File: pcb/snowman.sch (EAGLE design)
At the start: 15 parts, among them U1 ATTINY85-20PU

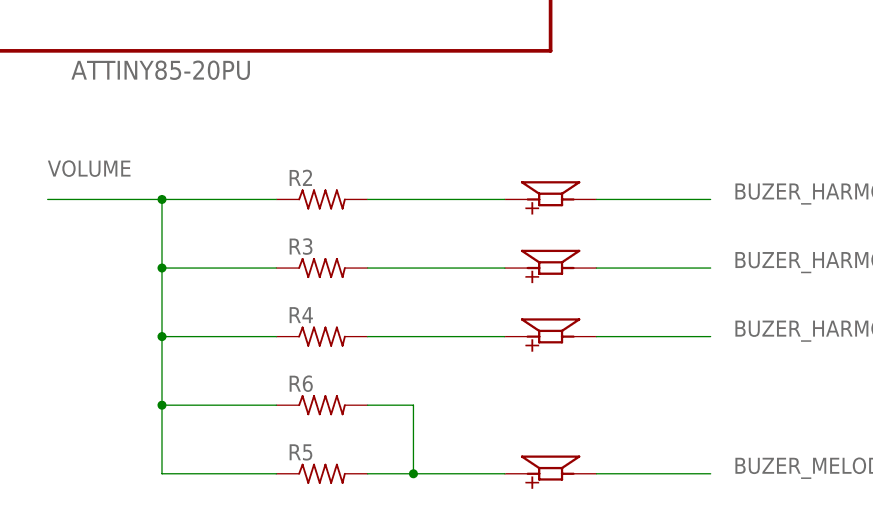
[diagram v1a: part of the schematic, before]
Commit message: add diode current filter to buzzers
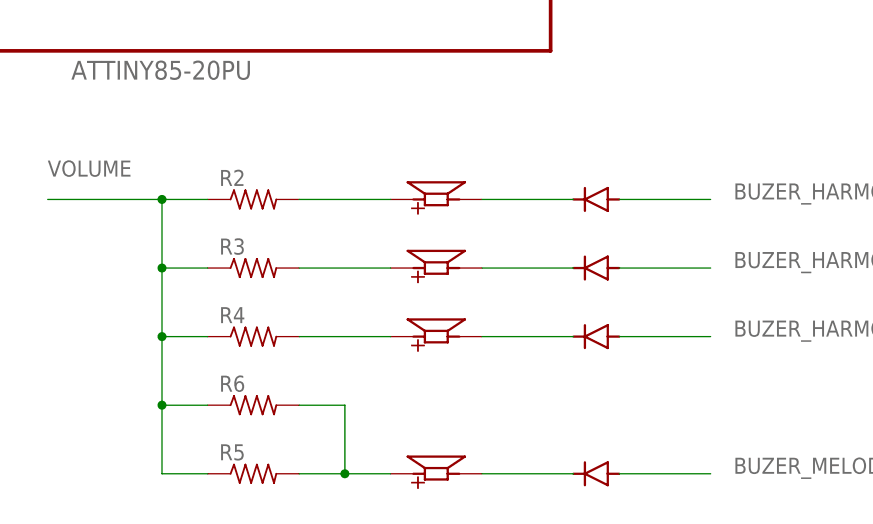
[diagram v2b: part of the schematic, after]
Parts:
- added D1, D2, D3, D4: GF1, diode:GF1
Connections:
- new net N$10: D1.C, LS1.N
- new net N$7: D4.C, LS2.N
- new net N$8: D3.C, LS4.N
- new net N$9: D2.C, LS3.N
- net BUZER_HARMONY_1: now also D4.A; no longer LS2.N
- net BUZER_HARMONY_2: now also D3.A; no longer LS4.N
- net BUZER_HARMONY_3: now also D2.A; no longer LS3.N
- net BUZER_MELODY: now also D1.A; no longer LS1.N
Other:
- moved on the sheet: R2, R3, R4, R5, R6

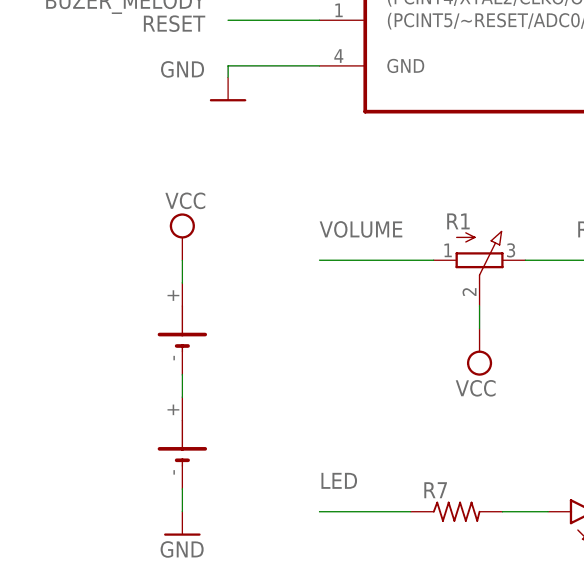
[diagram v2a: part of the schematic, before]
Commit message: replace component CR-AA -> BLOSSOM-BLM-18650-2PCS
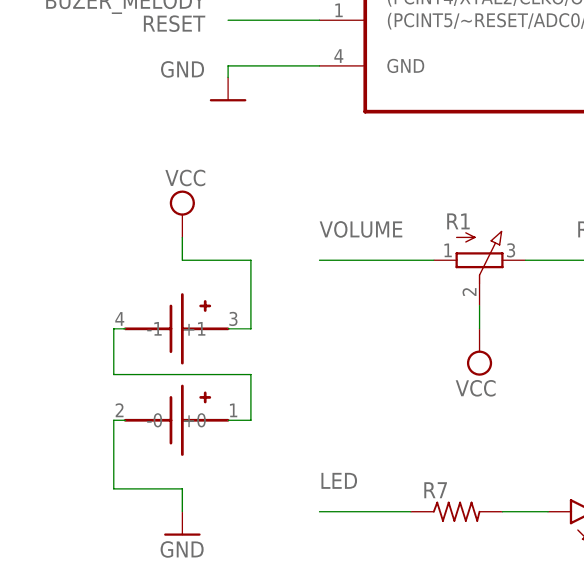
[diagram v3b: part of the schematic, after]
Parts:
- removed G1, G2: CR-AA, battery:CR-AA
- added U$1: BLOSSOM-BLM-18650-2PCS, battery-holders:BLOSSOM-BLM-18650-2PCS
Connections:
- removed net N$1: G1.-, G2.+
- new net N$12: U$1.+0, U$1.-1
- net GND: now also U$1.-0; no longer G2.-
- net VCC: now also U$1.+1; no longer G1.+
